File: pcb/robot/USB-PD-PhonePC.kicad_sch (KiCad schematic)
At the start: 3 parts, among them J9 Conn_01x16

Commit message: Re-unify USB-PD module into main board (single-PCB architecture) (#17)
Merges the USB-PD module circuitry back into the main robot board as
a single PCB, reversing the earlier main-board/USB-PD-daughter-board
split. Full re-route and re-placement of the combined design:

- Consolidated low-profile parts toward the board center, using the
  space freed up by relocated capacitors, for better overall use of
  the available area.
- Kept all 0-ohm test/isolation jumpers in accessible locations for
  bench testing.
- Added/corrected footprints for several parts that had broken or
  incorrect footprints (DDC6_TEX variants, SOT-23-6, SOT-23-3,
  R0402).

Carries forward every closed correction issue and update made since
the original split: #3 (CC jumpers), #6 (IC1.ON pull-down), #14/#15
(ADC divider, motor connector pinout), #16, #18 (I2C isolation
jumpers), #19 (charger-sense GPIO interrupt), plus the BOM/pricing
updates, LED changes, and MAX77642 replacement.

Verified via kicad-cli ERC/DRC + netlist diff against the pre-merge
board: 0 unconnected items (unchanged), no new DRC error-level
violations besides one pre-existing excluded item, and the #6
(IC1.ON pull-down) and #19 (charger-sense GPIO interrupt) circuits
confirmed intact at the net-topology level despite the full-board
re-annotation changing most reference designators. Most of the raw
diff size is a KiCad 9 footprint-format upgrade (pre-2023 format
rewritten to current) rather than design changes - spot-checked
against unrelated footprints (e.g. mounting holes), which show
identical geometry under the new syntax.
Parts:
- added C10, C21, C22: 4.7uF, robot:C_0603_1608Metric, symbol robot:C
- added C11, C12: 27pF, robot:C_0402_1005Metric, symbol robot:C
- added C13, C14, C16, C17, C18, C19, C20: 1uF, robot:C_0402_1005Metric, symbol robot:C
- added C15: 2.2uF, robot:C_0603_1608Metric, symbol robot:C
- added J1: USB4151-GF-C, robot:GCT_USB4151-GF-C_REVA, symbol robot:USB4151-GF-C_REVA
- added L2: 0.47uH, robot:Vishay-IHLP-2020BZ-FP_1.905x2.79-3D_2.0-0-0-MFG, symbol robot:INDUCTOR
- added NT5, NT6: NetTie_2, robot:NetTie-_SMD_Pad6mil, symbol robot:NetTie_2
- added R31, R33: 120k, robot:R_0603_1608Metric, symbol robot:R
- added R32, R34: 649k, robot:R_0603_1608Metric, symbol robot:R
- added R35, R36, R39, R52: 0, robot:R_0603_1608Metric, symbol robot:R
- added R37, R38: 10, robot:R_0402_1005Metric, symbol robot:R
- added R40, R45: 0, robot:R_0805_2012Metric, symbol robot:R
- added R41: 422, robot:R_0402_1005Metric, symbol robot:RC0402FR-07422RL
- added R42: 100, robot:R_0402_1005Metric, symbol robot:RC0402FR-07100RL
- added R43, R44: 2.2k, robot:R_0603_1608Metric, symbol robot:R
- added R46: 100k, robot:R_0603_1608Metric, symbol robot:R
- added R47: DNP, robot:R_0603_1608Metric, symbol robot:R
- added R48: 0, robot:R_0603_1608Metric_3pin_Switch, symbol robot:Switch_R_SMD_3pin
- added R49: 200k, robot:R_0603_1608Metric, symbol robot:R
- added S2: JS202011JCQN, robot:SW_JS202011JCQN, symbol robot:JS202011SCQN
- added TP14, TP15, TP16, TP17, TP18, TP19, TP20, TP21, TP22: SMD_0603, robot:TestPoint_SMD_0603, symbol robot:TestPoint
- added U10, U5, U7, U9: TPD1E05U06, robot:TPD1E05U06DPYR, symbol robot:TPD1E05U06_1
- added U11: MAX77958EWV+T, robot:MAX77958EWV&plus_T, symbol robot:MAX77958EWV+T
- added U12: TPS22950CDDCR, DDC6_TEX, symbol robot:TPS22950CDDCR
- added U13: TPS61253AYFFT, robot:Texas_Instruments-YFF0009-BGA9C40P3X3_119X129X62, symbol robot:TPS61253AYFFR
- added U4, U8: TPD1E05U06, robot:TPD1E05U06DPYR, symbol robot:TPD1E05U06
- added U6: TVS0500DRV, robot:TVS0500DRVR, symbol robot:TVS0500DRV
- J2: renamed from J9; symbol Connector_Generic:Conn_01x16 -> robot:Conn_01x16; now not fitted
- R50: renamed from R73; symbol Device:R -> robot:R
- R51: renamed from R65; symbol Device:R -> robot:R
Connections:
- net AGND: now also C11.2, C12.2, C13.2, C15.2, C16.2, C18.2, C19.2, C20.2, R48.1, U10.2 (GND), U11.C5 (GND_A), U11.D4 (GPIO6), U11.D6 (GND_D), U4.2 (GND), U5.2 (GND), U7.2 (GND), U8.2 (GND), U9.2 (GND)
- net DN1: now also S2.1
- net DP1: now also S2.4
- net INTB_SL: now also R49.2, TP21.1, U11.A1 (INTB)
- net SCL_M: now also J2.7 (Pin_7), R51.2; no longer R50.1
- net SCL_SL: now also U11.B2 (SCL)
- net SDA_M: now also J2.8 (Pin_8), R50.2; no longer R51.1
- net SDA_SL: now also U11.B3 (SDA)
- net USB_Phone_SYS: now also R39.1, R52.2
- net VCIN: now also C13.1, U11.A5 (VCIN)
- net VIO1: now also C20.1, R49.1, U11.B1 (VIO1)
- net VIO2: now also C19.1, R43.1, R44.1, R48.3, U11.C1 (VIO2)
- net PGND renamed GND
- net GND: now also C10.2, C14.2, C17.2, C21.2, C22.2, J1.A1 (GND), J1.A12 (GND), J1.B1 (GND), J1.B12 (GND), J1.S1 (SHIELD), J1.S2 (SHIELD), J1.S3 (SHIELD), J1.S4 (SHIELD), J1.S5 (SHIELD), R41.2, R46.2, R47.2, U12.3 (GND), U13.C1 (GND), U13.C2 (GND), U6.1 (GND), U6.2 (GND), U6.3 (GND), U6.7 (GND)
- new net: R44.2, R51.1, U11.C2 (SCL_M)
- new net: R41.1, U12.4 (ILIM)
- new net: C17.1, NT5.1, U11.A6 (VBUS)
- new net: C14.1, R39.2, U11.B6 (SYS)
- new net: J1.B5 (CC2), R36.1, TP17.1, U7.1 (I/O)
- new net: C11.1, R36.2, U11.A4 (CC2)
- new net: J1.A8 (SBU1), R33.2, U5.1 (I/O)
- new net: C15.1, U11.C6 (AVL)
- new net: C22.1, L2.1, NT6.2, R52.1
- new net: J1.A5 (CC1), R35.1, TP16.1, U9.1 (I/O)
- new net: C12.1, R35.2, U11.A3 (CC1)
- new net: C16.1, U11.A2 (VDD1P1)
- new net: R42.1, TP18.1, U12.1 (ON)
- new net: C18.1, U11.B5 (VDD1P8)
- new net: J1.B8 (SBU2), R31.2, U4.1 (I/O)
- new net: L2.2, U13.B1 (SW), U13.B2 (SW)
- new net: R48.2, U13.C3 (MODE)
- new net: R43.2, R50.1, U11.C3 (SDA_M)
- new net: NT6.1, U13.A3 (VIN)
- new net DIFF_EXT_N: J1.A7 (DN1), J1.B7 (DN2), R38.1, S2.2, TP14.1, U8.1 (I/O)
- new net DIFF_EXT_P: J1.A6 (DP1), J1.B6 (DP2), R37.1, S2.5, TP15.1, U10.1 (I/O)
- new net DIFF_EXT_PR_N: R38.2, U11.D1 (DN)
- new net DIFF_EXT_PR_P: R37.2, U11.D2 (DP)
- new net DIFF_SWITCHED_N: S2.3, TP19.1, U11.E1 (DN1)
- new net DIFF_SWITCHED_P: S2.6, TP20.1, U11.E2 (DP2)
- new net GPIO0: R33.1, R34.2, U11.E6 (GPIO0)
- new net GPIO1: R31.1, R32.2, U11.B4 (GPIO1)
- new net GPIO3: R32.1, R34.1, U11.D5 (GPIO3)
- new net GPIO4: R42.2, U11.E4 (GPIO4)
- new net GPIO5: TP22.1, U11.E3 (GPIO5), U13.B3 (EN)
- new net NET A1- R74: C21.1, R45.2, R46.1, R47.1, U13.A1 (VOUT), U13.A2 (VOUT)
- new net NET VIN-R74: R45.1, U12.2 (VIN)
- new net VBUS_Phone: C10.1, J1.A4 (VBUS), J1.A9 (VBUS), J1.B4 (VBUS), J1.B9 (VBUS), R40.2, U6.4 (IN), U6.5 (IN), U6.6 (IN)
- new net VBUS_Phone_PS: NT5.2, R40.1, U12.5 (VOUT)
- no-connect marks 1 -> 13
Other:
- note added: "Enable takes 500 us or so. For FRS you need to be less than 150 So GPIO0 needs to be on prior to the FRS request is sent."
- note added: "Looks like VIN_5V pulls up to 16 mA to program the MTP whereas all other power comes from SYS or VBUS with VBUS taking precedence"
- note added: "Move both jumpers to toggle between directly connecting USB port D+/- with MCU vs gated."
- note added: "NOTE: Only ONE of R3 (CC1) / R4 (CC2) should be populated for a direct male USB-C plug configuration. Default: R3 populated, R4 DNP. The unused CC-position contact must remain floating - do NOT tie it to 5V, GND, Rp, Rd, or the other CC line."
- note added: "Pull ups based on single slave device and reducing power consumption."
- note added: "This should be kept low else back currents can occur Only test Forced PWM or Ultrasonic if you ensure no source present on VOUT"
- moved on the sheet: R50, R51

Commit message: Remove leftover Conn_01x16, tidy up hierarchical labels (fixes #21)
Deleted J2, the old castellated-edge connector placeholder left over from when USB-PD was a separate board - it's been DNP/off-board since the reunification and wasn't even in the netlist, so nothing to reroute. Reconnected the signals that used to fan into it (USB_Phone_SYS, PGND, VCIN, SCL_M/SDA_M, INTB_SL, AGND, VIO1/VIO2, SCL_SL/SDA_SL, DP1/DN1) with proper hierarchical labels instead. Checked ERC/DRC before and after: same connectivity, 0 unconnected items, no new violations - the only thing that dropped off was the "footprint not in library" warning J2 itself used to trigger.
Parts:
- removed J2: Conn_01x16, robot:SMD FOR CASTELLATED 1x16 2.54mm, symbol robot:Conn_01x16
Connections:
- no-connect marks 13 -> 12
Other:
- note removed: "AGND"
- note removed: "DN1"
- note removed: "DP1"
- note removed: "INTB_SL"
- note removed: "PGND"
- note removed: "SCL_M"
- note removed: "SCL_SL"
- note removed: "SDA_M"
- note removed: "SDA_SL"
- note removed: "This is the connector for the new external USB PD Phone module."
- note removed: "USB_Phone_SYS"
- note removed: "VCIN"
- note removed: "VIO1"
- note removed: "VIO2"

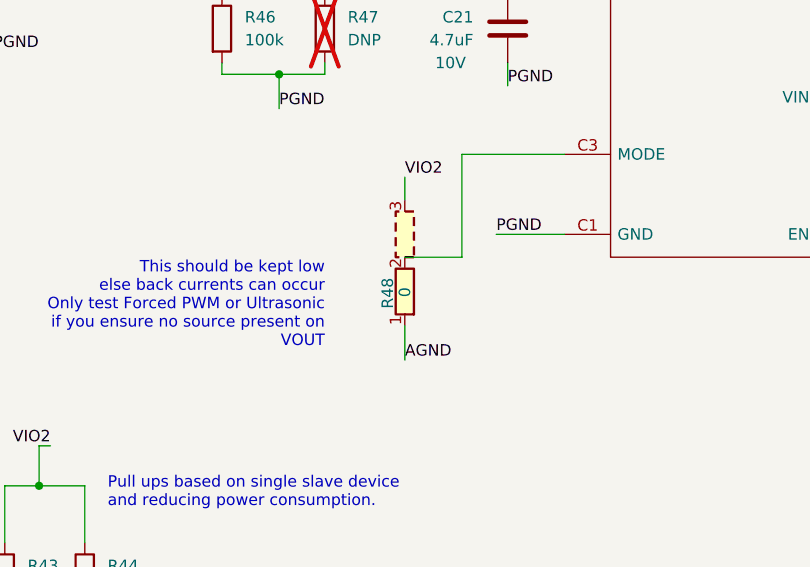
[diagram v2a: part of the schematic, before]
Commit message: Clean up BOM fields, regenerate gerbers/BOM/CPL for fab order (#17)
MPN -> Part Number field rename on a few parts in Protection.kicad_sch
and USB-PD-PhonePC.kicad_sch for consistent BOM output. R48 value
0 -> S0 (it's the 3-pin switch footprint, not a real resistor value).
Re-exported gerbers, drill files, BOM and CPL for the JLCPCB
fab+assembly order just placed.
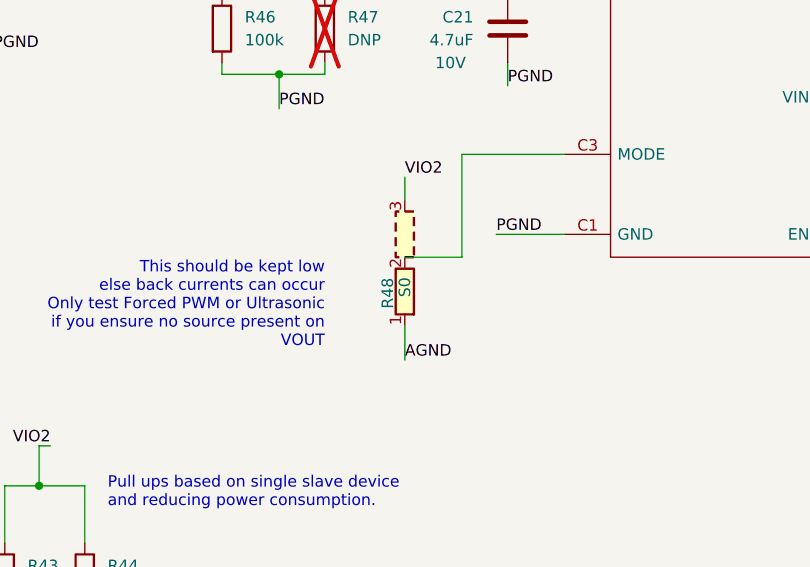
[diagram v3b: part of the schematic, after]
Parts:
- R41: MP RC0402FR-07422RL -> (none); Part Number (none) -> RC0402FR-07422RL
- R42: MP RC0402FR-07100RL -> (none); Part Number (none) -> RC0402FR-07100RL
- R48: value 0 -> S0
- U12: Part Number (none) -> TPS22950CDDCR
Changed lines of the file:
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@@
 			)
 		)
-		(property "MP" "RC0402FR-07422RL"
+		(property "Part Number" "RC0402FR-07422RL"
 			(at 288.29 107.95 0)
 			(effects
@@
 			)
 		)
-		(property "MP" "RC0402FR-07100RL"
+		(property "Part Number" "RC0402FR-07100RL"
 			(at 332.74 82.55 0)
 			(effects
@@
 			)
 		)
-		(property "Value" "0"
+		(property "Value" "S0"
 			(at 379.73 132.715 90)
 			(effects
@@
 			(at 328.93 93.98 0)
 			(effects
+				(font
+					(size 1.27 1.27)
+				)
+				(hide yes)
+			)
+		)
+		(property "Part Number" "TPS22950CDDCR"
+			(at 328.93 93.98 0)
+			(effects
